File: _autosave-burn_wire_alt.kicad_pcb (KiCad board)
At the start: 2 copper layers, 23 x 24.5 mm, 14 parts, among them J1 TestPoint_THTPad_1.0x1.0mm_Dr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, J2 TestPoint_THTPad_1.0x1.0mm_Dr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, U1 ADP2303ARDZ

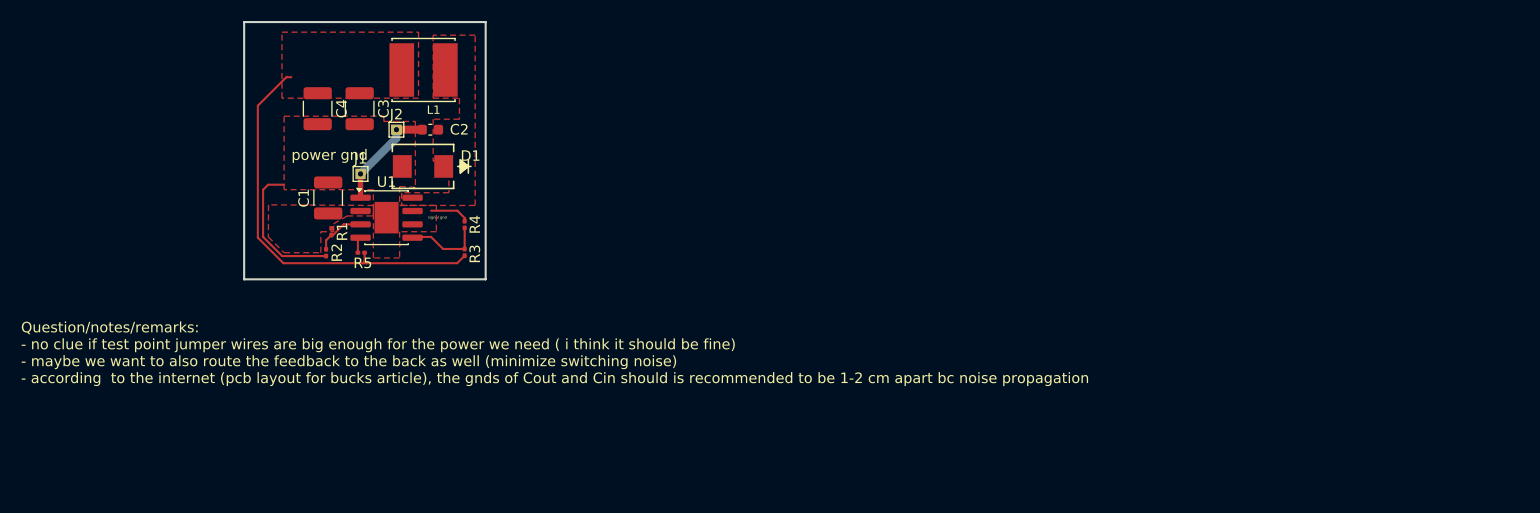
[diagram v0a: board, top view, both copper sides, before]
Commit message: moved fb away from sw
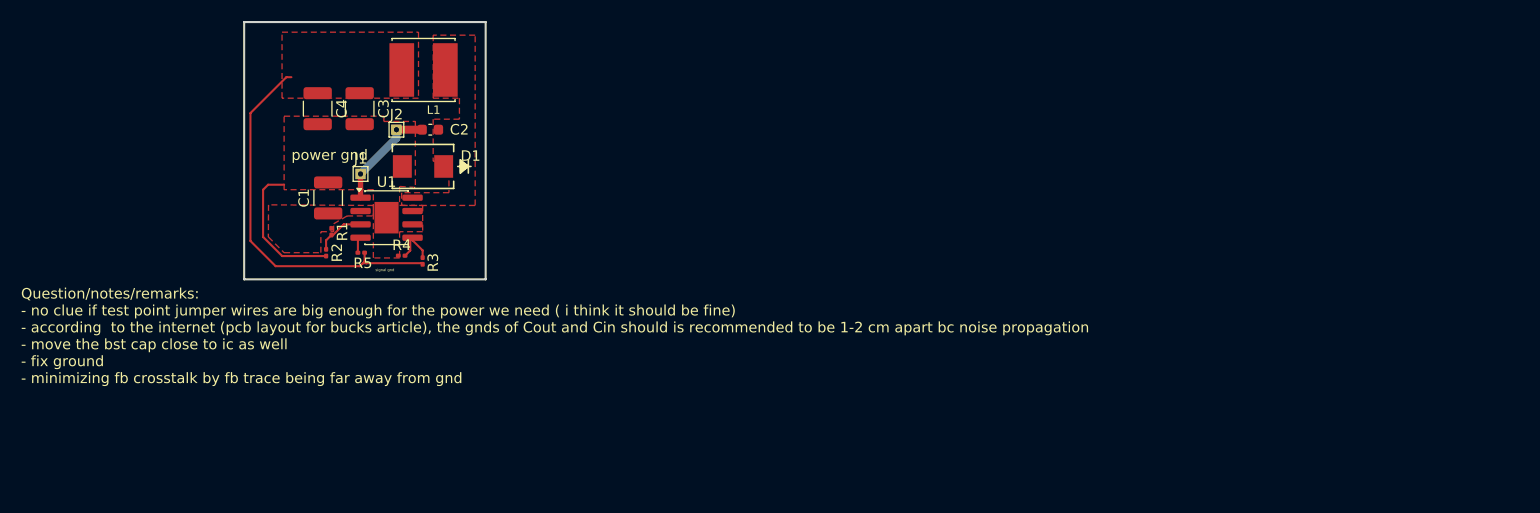
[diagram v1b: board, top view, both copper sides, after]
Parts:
- moved R4 6.69 mm to (172.0, 98.0), turned to 180 degrees
- moved R3 4.08 mm to (174.0, 98.5)
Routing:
- net GND: track 17.2 -> 13.5 mm
- net /FB: track 7.37 -> 4.30 mm
- net /Vout: track 39.2 -> 36.4 mm
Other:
- board text added: "Question/notes/remarks: - no clue if test point jumper wires are big enough for the power we need ( i think it should be fine) - according to the internet (pcb layout for bucks article), the gnds of Cout and Cin should is recommended to be 1-2 cm apart bc noise propagation - move the bst cap close to ic as well - fix ground - minimizing fb crosstalk by fb trace being far away from gnd"
- board text removed: "Question/notes/remarks: - no clue if test point jumper wires are big enough for the power we need ( i think it should be fine) - maybe we want to also route the feedback to the back as well (minimize switching noise) - according to the internet (pcb layout for bucks article), the gnds of Cout and Cin should is recommended to be 1-2 cm apart bc noise propagation"
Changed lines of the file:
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@@
 	(footprint "Resistor_SMD:R_0201_0603Metric"
 		(layer "F.Cu")
-		(at 178 97.68 90)
+		(at 174 98.5 90)
 		(descr "Resistor SMD 0201 (0603 Metric), square (rectangular) end terminal, IPC-7351 nominal, (Body size source: https://www.vishay.com/docs/20052/crcw0201e3.pdf)")
 		(tags "resistor")
@@
 	(footprint "Resistor_SMD:R_0201_0603Metric"
 		(layer "F.Cu")
-		(at 178 95.03487 90)
+		(at 172 98 180)
 		(descr "Resistor SMD 0201 (0603 Metric), square (rectangular) end terminal, IPC-7351 nominal, (Body size source: https://www.vishay.com/docs/20052/crcw0201e3.pdf)")
 		(tags "resistor")
 		(property "Reference" "R4"
-			(at 0 1 90)
+			(at 0 1 0)
 			(layer "F.SilkS")
 			(effects
@@
 		)
 		(property "Value" "10k"
-			(at 0 1.05 90)
+			(at 0 1.05 0)
 			(layer "F.Fab")
 			(hide yes)
@@
 		)
 		(property "Datasheet" ""
-			(at 0 0 90)
+			(at 0 0 0)
 			(layer "F.Fab")
 			(hide yes)
@@
 		)
 		(property "Description" "Resistor, US symbol"
-			(at 0 0 90)
+			(at 0 0 0)
 			(layer "F.Fab")
 			(hide yes)
@@
 		)
 		(property "KiLib_Generator" "SMD_2terminal_chip_molded"
-			(at 0 0 90)
+			(at 0 0 0)
 			(layer "F.SilkS")
 			(hide yes)
@@
 		)
 		(fp_text user "${REFERENCE}"
-			(at 0 -0.68 90)
+			(at 0 -0.68 0)
 			(layer "F.Fab")
 			(effects
@@
 		)
 		(pad "" smd roundrect
-			(at -0.345 0 90)
+			(at -0.345 0 180)
 			(size 0.318 0.36)
 			(layers "F.Paste")
@@
 		)
 		(pad "" smd roundrect
-			(at 0.345 0 90)
+			(at 0.345 0 180)
 			(size 0.318 0.36)
 			(layers "F.Paste")
@@
 		)
 		(pad "1" smd roundrect
-			(at -0.32 0 90)
+			(at -0.32 0 180)
 			(size 0.46 0.4)
 			(layers "F.Cu" "F.Mask")
@@
 		)
 		(pad "2" smd roundrect
-			(at 0.32 0 90)
+			(at 0.32 0 180)
 			(size 0.46 0.4)
 			(layers "F.Cu" "F.Mask")
@@
 	)
 	(gr_text "signal gnd"
-		(at 174.5 94.5 0)
+		(at 169.5 99.5 0)
 		(layer "F.SilkS")
 		(effects
@@
 		)
 	)
-	(gr_text "Question/notes/remarks:\n- no clue if test point jumper wires are big enough for the power we need ( i think it should be fine)\n- maybe we want to also route the feedback to the back as well (minimize switching noise)\n- according  to the internet (pcb layout for bucks article), the gnds of Cout and Cin should is recommended to be 1-2 cm apart bc noise propagation"
+	(gr_text "Question/notes/remarks:\n- no clue if test point jumper wires are big enough for the power we need ( i think it should be fine)\n- according  to the internet (pcb layout for bucks article), the gnds of Cout and Cin should is recommended to be 1-2 cm apart bc noise propagation\n- move the bst cap close to ic as well\n- fix ground\n- minimizing fb crosstalk by fb trace being far away from gnd"
 		(at 135.75 110.25 0)
 		(layer "F.SilkS")
@@
 	)
 	(segment
-		(start 158.30513 83.71487)
-		(end 158.30513 96.280555)
+		(start 168.47013 98.54987)
+		(end 168.63513 98.71487)
+		(width 0.2)
+		(layer "F.Cu")
+		(net "/Vout")
+	)
+	(segment
+		(start 168.47013 97.71487)
+		(end 168.47013 98.54987)
 		(width 0.2)
 		(layer "F.Cu")
@@
 	)
 	(segment
-		(start 168.47013 98.54987)
+		(start 168.02 99)
+		(end 168.30513 98.71487)
+		(width 0.2)
+		(layer "F.Cu")
+		(net "/Vout")
+	)
+	(segment
+		(start 157.6 96.6)
+		(end 160 99)
+		(width 0.2)
+		(layer "F.Cu")
+		(net "/Vout")
+	)
+	(segment
+		(start 160 99)
+		(end 168.02 99)
+		(width 0.2)
+		(layer "F.Cu")
+		(net "/Vout")
+	)
+	(segment
+		(start 173.89487 98.71487)
 		(end 168.63513 98.71487)
-		(width 0.2)
-		(layer "F.Cu")
-		(net "/Vout")
-	)
-	(segment
-		(start 168.47013 97.71487)
-		(end 168.47013 98.54987)
-		(width 0.2)
-		(layer "F.Cu")
-		(net "/Vout")
-	)
-	(segment
-		(start 177.28513 98.71487)
-		(end 168.63513 98.71487)
-		(width 0.2)
-		(layer "F.Cu")
-		(net "/Vout")
-	)
-	(segment
-		(start 161.02 81)
-		(end 158.30513 83.71487)
-		(width 0.2)
-		(layer "F.Cu")
-		(net "/Vout")
-	)
-	(segment
-		(start 160.739445 98.71487)
-		(end 168.30513 98.71487)
-		(width 0.2)
-		(layer "F.Cu")
-		(net "/Vout")
-	)
-	(segment
-		(start 158.30513 96.280555)
-		(end 160.739445 98.71487)
 		(width 0.2)
 		(layer "F.Cu")
@@
 	)
 	(segment
-		(start 178 98)
-		(end 177.28513 98.71487)
+		(start 157.6 84.42)
+		(end 157.6 96.6)
+		(width 0.2)
+		(layer "F.Cu")
+		(net "/Vout")
+	)
+	(segment
+		(start 174 98.82)
+		(end 173.89487 98.71487)
+		(width 0.2)
+		(layer "F.Cu")
+		(net "/Vout")
+	)
+	(segment
+		(start 161.02 81)
+		(end 157.6 84.42)
 		(width 0.2)
 		(layer "F.Cu")
@@
 		(start 158.80513 96.21487)
 		(end 158.80513 91.71487)
-		(width 0.2)
-		(layer "F.Cu")
-		(net "GND")
-	)
-	(segment
-		(start 178 94.40974)
-		(end 177.30513 93.71487)
-		(width 0.2)
-		(layer "F.Cu")
-		(net "GND")
-	)
-	(segment
-		(start 178 94.71487)
-		(end 178 94.40974)
-		(width 0.2)
-		(layer "F.Cu")
-		(net "GND")
-	)
-	(segment
-		(start 177.30513 93.71487)
-		(end 174.80513 93.71487)
 		(width 0.2)
 		(layer "F.Cu")
@@
 	)
 	(segment
-		(start 178 97.36)
-		(end 175.95026 97.36)
+		(start 173.036611 96.28561)
+		(end 173.036611 96.536611)
 		(width 0.2)
 		(layer "F.Cu")
@@
 	)
 	(segment
-		(start 175.95026 97.36)
-		(end 174.80513 96.21487)
+		(start 172.82 97.5)
+		(end 172.82 96.502221)
 		(width 0.2)
 		(layer "F.Cu")
@@
 	)
 	(segment
-		(start 174.80513 96.21487)
-		(end 173.107351 96.21487)
+		(start 173.036611 96.536611)
+		(end 174 97.5)
 		(width 0.2)
 		(layer "F.Cu")
@@
 	)
 	(segment
-		(start 178 95.35487)
-		(end 178 97.36)
+		(start 172.32 98)
+		(end 172.82 97.5)
+		(width 0.2)
+		(layer "F.Cu")
+		(net "/FB")
+	)
+	(segment
+		(start 174 97.5)
+		(end 174 98.18)
+		(width 0.2)
+		(layer "F.Cu")
+		(net "/FB")
+	)
+	(segment
+		(start 172.82 96.502221)
+		(end 173.036611 96.28561)
 		(width 0.2)
 		(layer "F.Cu")
@@
 			(pts
 				(xy 160.80513 84.71487) (xy 170.30513 84.71487) (xy 170.30513 85.21487) (xy 173.303711 85.21487)
-				(xy 173.304518 91.5) (xy 171.80513 91.409245) (xy 171.80513 93.208563) (xy 175.30513 93.21487) (xy 175.30513 95.71487)
+				(xy 173.304518 91.5) (xy 171.80513 91.409245) (xy 171.80513 93.208563) (xy 174 93.212518) (xy 174 95.71487)
 				(xy 171.80513 95.71487) (xy 171.80513 98.21487) (xy 169.30513 98.21487) (xy 169.30513 91.71487)
 				(xy 160.80513 91.71487)

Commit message: tweaks
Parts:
- moved J1 0.44 mm to (168.1, 90.7)
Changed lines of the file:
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@@
 	(footprint "TestPoint:TestPoint_THTPad_1.0x1.0mm_Drill0.5mm"
 		(layer "F.Cu")
-		(at 168.081839 90.21487)
+		(at 168.136714 90.651297)
 		(descr "THT rectangular pad as test Point, square 1.0mm side length, hole diameter 0.5mm")
 		(tags "test point THT pad rectangle square")
@@
 	)
 	(gr_text "signal gnd"
-		(at 169.5 99.5 0)
+		(at 169.5 97.5 0)
 		(layer "F.SilkS")
 		(effects
@@
 	)
 	(gr_text "power gnd"
-		(at 161.5 89 0)
+		(at 161 88.5 0)
 		(layer "F.SilkS")
 		(effects
@@
 	)
 	(segment
+		(start 164.80513 98.03487)
+		(end 160.62513 98.03487)
+		(width 0.2)
+		(layer "F.Cu")
+		(net "GND")
+	)
+	(segment
+		(start 159.28013 91.23987)
+		(end 160.80513 91.23987)
+		(width 0.2)
+		(layer "F.Cu")
+		(net "GND")
+	)
+	(segment
+		(start 158.80513 96.21487)
+		(end 158.80513 91.71487)
+		(width 0.2)
+		(layer "F.Cu")
+		(net "GND")
+	)
+	(segment
 		(start 158.80513 91.71487)
 		(end 159.28013 91.23987)
@@
 	)
 	(segment
-		(start 158.80513 96.21487)
-		(end 158.80513 91.71487)
-		(width 0.2)
-		(layer "F.Cu")
-		(net "GND")
-	)
-	(segment
-		(start 159.28013 91.23987)
-		(end 160.80513 91.23987)
-		(width 0.2)
-		(layer "F.Cu")
-		(net "GND")
-	)
-	(segment
-		(start 164.80513 98.03487)
-		(end 160.62513 98.03487)
-		(width 0.2)
-		(layer "F.Cu")
-		(net "GND")
-	)
-	(segment
 		(start 160.62513 98.03487)
 		(end 158.80513 96.21487)
@@
 		(layer "F.Cu")
 		(net "GND")
+	)
+	(segment
+		(start 168.136714 90.651297)
+		(end 168.081839 90.706172)
+		(width 0.508)
+		(layer "F.Cu")
+		(net "/BST")
 	)
 	(segment
@@
 	)
 	(segment
-		(start 168.081839 90.21487)
+		(start 168.081839 90.706172)
 		(end 168.081839 92.470838)
 		(width 0.508)
@@
 	)
 	(segment
+		(start 168.081839 90.596422)
+		(end 168.081839 90.5)
+		(width 0.762)
+		(layer "B.Cu")
+		(net "/BST")
+	)
+	(segment
 		(start 171.5 86.796709)
-		(end 168.081839 90.21487)
+		(end 168.136714 90.159995)
+		(width 0.762)
+		(layer "B.Cu")
+		(net "/BST")
+	)
+	(segment
+		(start 168.136714 90.159995)
+		(end 168.136714 90.651297)
+		(width 0.762)
+		(layer "B.Cu")
+		(net "/BST")
+	)
+	(segment
+		(start 168.136714 90.651297)
+		(end 168.081839 90.596422)
 		(width 0.762)
 		(layer "B.Cu")
@@
 		(polygon
 			(pts
-				(xy 160.80513 84.71487) (xy 170.30513 84.71487) (xy 170.30513 85.21487) (xy 173.303711 85.21487)
+				(xy 160.80513 84.71487) (xy 170.30513 84.71487) (xy 170.305137 84.71487) (xy 173.303604 84.71487)
 				(xy 173.304518 91.5) (xy 171.80513 91.409245) (xy 171.80513 93.208563) (xy 174 93.212518) (xy 174 95.71487)
 				(xy 171.80513 95.71487) (xy 171.80513 98.21487) (xy 169.30513 98.21487) (xy 169.30513 91.71487)
@@
 		(polygon
 			(pts
-				(xy 172 92) (xy 172 93.21487) (xy 179 93.21487) (xy 179 77) (xy 175 77) (xy 175 83) (xy 177.5 83)
-				(xy 177.5 85) (xy 175 85) (xy 175 89) (xy 176.5 89) (xy 176.5 92)
-			)
-		)
+				(xy 172 92) (xy 172 93.21487) (xy 179 93.21487) (xy 179 77) (xy 175 77) (xy 175 85) (xy 177.5 85)
+				(xy 175 85) (xy 175 92) (xy 176.5 92)
+			)
+		)

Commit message: added bst diode
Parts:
- added D2: D_Schottky, imported_footprints:CR_SMB_320-345BE_DIO-L, F.Cu at (164.7, 92.4)
- added J1: TestPoint_THTPad_1.0x1.0mm_Drill0.5mm, TestPoint:TestPoint_THTPad_1.0x1.0mm_Drill0.5mm, F.Cu at (164.7, 90.4)
- moved C1 4.50 mm to (160.5, 92.5)
- moved R1 0.82 mm to (166.0, 96.2)
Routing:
- net /BST: track 10.5 -> 14.2 mm
- net /Vout: track 36.4 -> 37.4 mm
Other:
- board size 23 x 24.5 mm -> 24.5 x 24.5 mm
- board text added: "Question/notes/remarks: - no clue if test point jumper wires are big enough for the power we need ( i think it should be fine) - according to the internet (pcb layout for bucks article), the gnds of Cout and Cin should is recommended to be 1-2 cm apart bc noise propagation - move the bst cap close to ic as well - fix ground - minimizing fb crosstalk by fb trace being far away from gnd - don't thi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"
- board text removed: "Question/notes/remarks: - no clue if test point jumper wires are big enough for the power we need ( i think it should be fine) - according to the internet (pcb layout for bucks article), the gnds of Cout and Cin should is recommended to be 1-2 cm apart bc noise propagation - move the bst cap close to ic as well - fix ground - minimizing fb crosstalk by fb trace being far away from gnd"
